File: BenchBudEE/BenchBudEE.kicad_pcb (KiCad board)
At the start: 4 copper layers, 165.1 x 63.5 mm, 57 parts, among them K1 1461069-5, P1 24 Pin MiniFit JR, P2 CONN_3X2, P3 CONN_2, P4 12 Pin Terminal Block, P5 3 Pin TB, Q1 2N3904, U1 LTV-816S, U2 MCP3901, U3 LMT84, U4 OPA4170

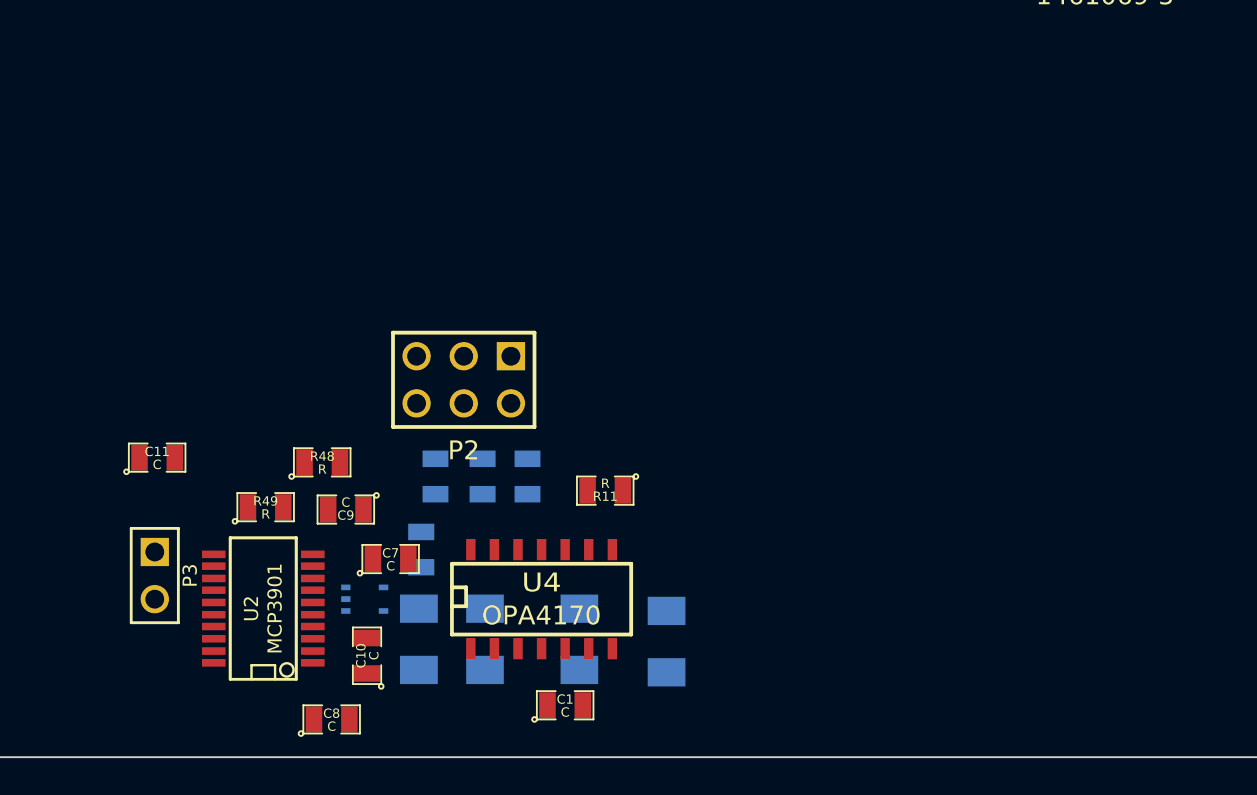
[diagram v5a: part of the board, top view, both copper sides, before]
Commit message: Roughly placed the current/fan driver module components.
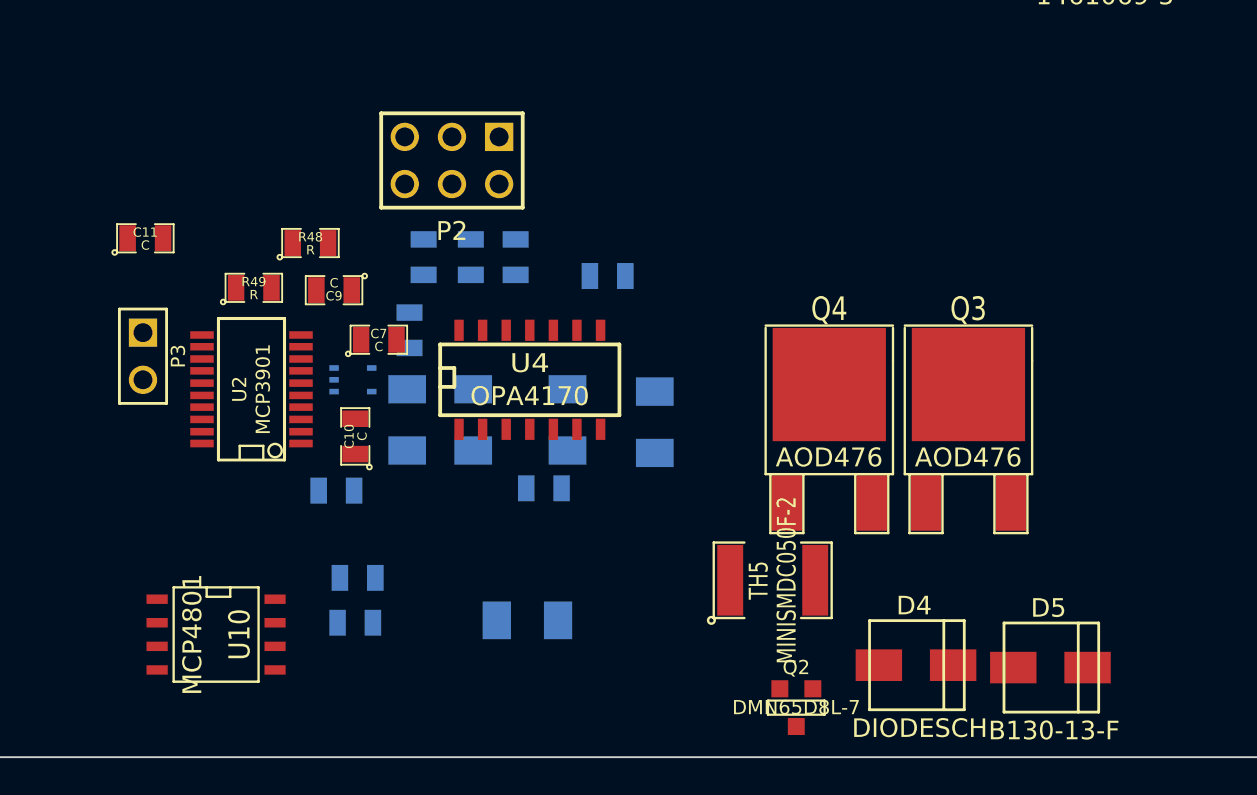
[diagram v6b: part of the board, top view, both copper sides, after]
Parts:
- added C13: C, SM0805, B.Cu at (183.0, 169.3)
- added D4: DIODESCH, SMA, F.Cu at (211.2, 171.6)
- added D5: B130-13-F, SMA, F.Cu at (218.4, 171.7)
- added Q2: DMN65D8L-7, SOT23GDS, F.Cu at (206.8, 173.9)
- added Q3: AOD476, DPAK2, F.Cu at (216.0, 162.8)
- added Q4: AOD476, DPAK2, F.Cu at (208.5, 162.8)
- added R24: R, SM0805, B.Cu at (183.1, 166.9)
- added R25: R, SM1206, B.Cu at (192.3, 169.2)
- added TH5: MINISMDC050F-2, SM1812, F.Cu at (205.5, 167.0)
- added U10: MCP4801, SO8N, F.Cu at (175.5, 169.9)
- C1, C8, R11: moved to B.Cu
- moved C8 12.3 mm to (182.0, 162.2)
- moved C11 11.8 mm to (171.7, 148.6)
- moved C7 11.8 mm to (184.3, 154.1)
- moved C9 11.8 mm to (181.9, 151.4)
- moved P2 11.8 mm to (188.2, 144.4)
- moved P3 11.8 mm to (171.6, 154.9)
- moved R10 11.8 mm to (189.4, 158.4)
- moved R12 11.8 mm to (186.7, 149.6)
- moved R13 11.8 mm to (185.9, 153.5)
- moved R44 11.8 mm to (191.6, 149.6)
- moved R45 11.8 mm to (189.2, 149.6)
- moved R48 11.8 mm to (180.6, 148.8)
- moved R49 11.8 mm to (177.5, 151.3)
- moved R7 11.8 mm to (194.4, 158.4)
- moved R8 11.8 mm to (185.8, 158.4)
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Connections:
- net /Arduino/ADC_CS_N renamed /Arduino/~ADC_CS
- ARD1 pad 13: (no net) -> N-0000059
- ARD1 pad 14: (no net) -> N-0000054

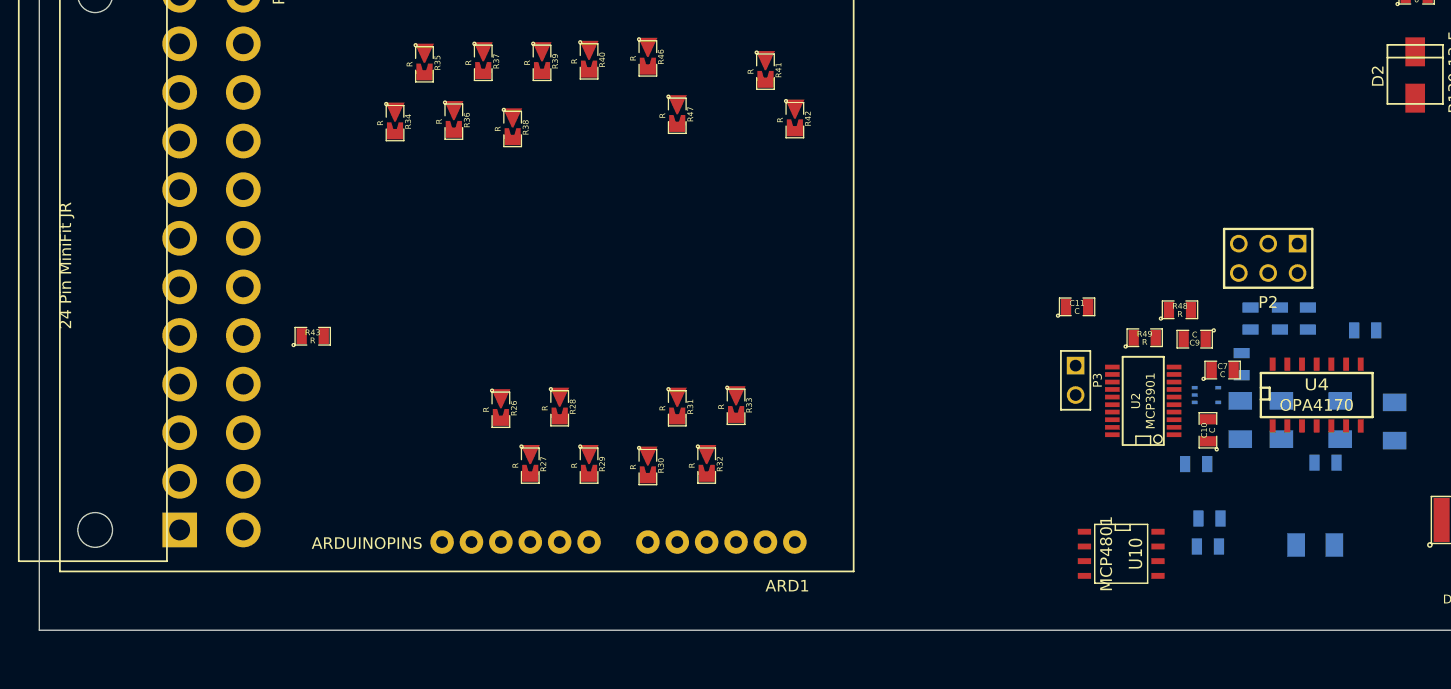
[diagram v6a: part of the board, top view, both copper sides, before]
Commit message: Roughly placed components for the Power Protection and Filtering module.
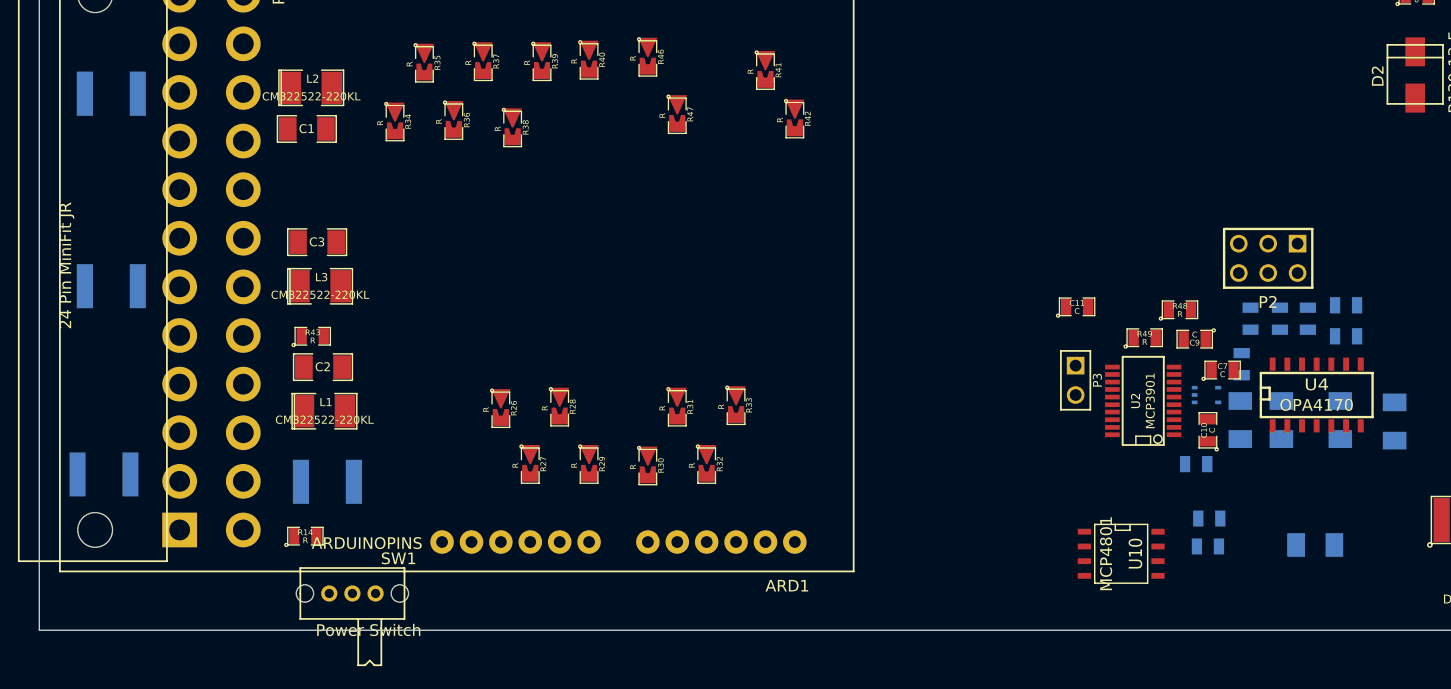
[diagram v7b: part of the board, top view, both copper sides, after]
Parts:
- added C2: C, SM1206, F.Cu at (106.6, 153.8)
- added C3: C, SM1206, F.Cu at (106.0, 143.0)
- added C6: C, SM0805, B.Cu at (194.9, 151.1)
- added L1: CM322522-220KL, SM1210L, F.Cu at (106.7, 157.6)
- added L2: CM322522-220KL, SM1210L, F.Cu at (105.5, 129.7)
- added L3: CM322522-220KL, SM1210L, F.Cu at (106.3, 146.8)
- added R14: R, SM0805, F.Cu at (105.0, 168.4)
- added SW1: Power Switch, BB_switch, F.Cu at (109.1, 173.4)
- added TH1: MINISMDC050F-2, SM1812, B.Cu at (87.6, 163.1)
- added TH2: MINISMDC050F-2, SM1812, B.Cu at (88.3, 146.8)
- added TH3: MINISMDC050F-2, SM1812, B.Cu at (88.3, 130.2)
- added TH4: MINISMDC050F-2, SM1812, B.Cu at (106.9, 163.7)
- C1: footprint SM0805 -> SM1206; moved to F.Cu
- moved C1 92.6 mm to (105.2, 133.2), turned to 180 degrees
- moved R11 2.72 mm to (194.9, 148.5)

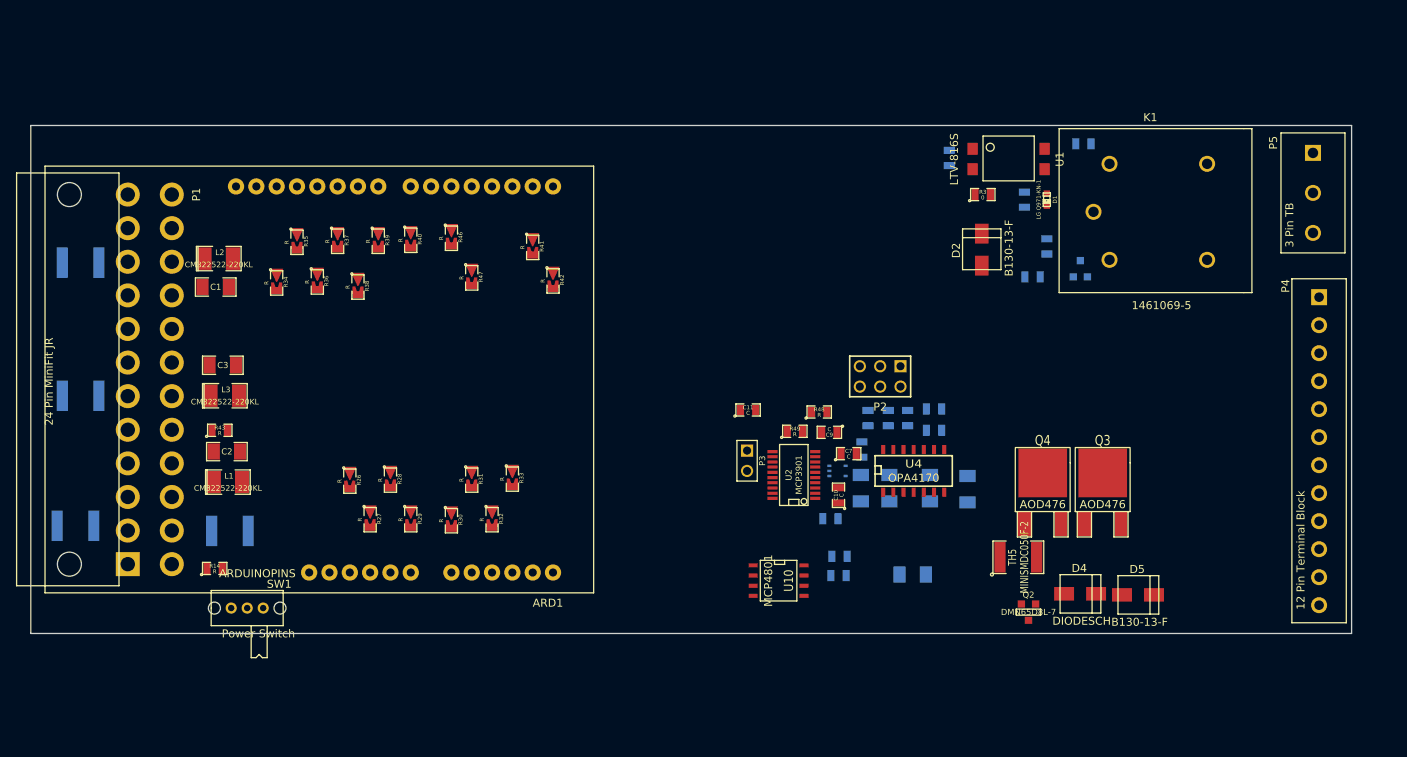
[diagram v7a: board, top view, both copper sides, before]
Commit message: Roughly placed the power modification module components.
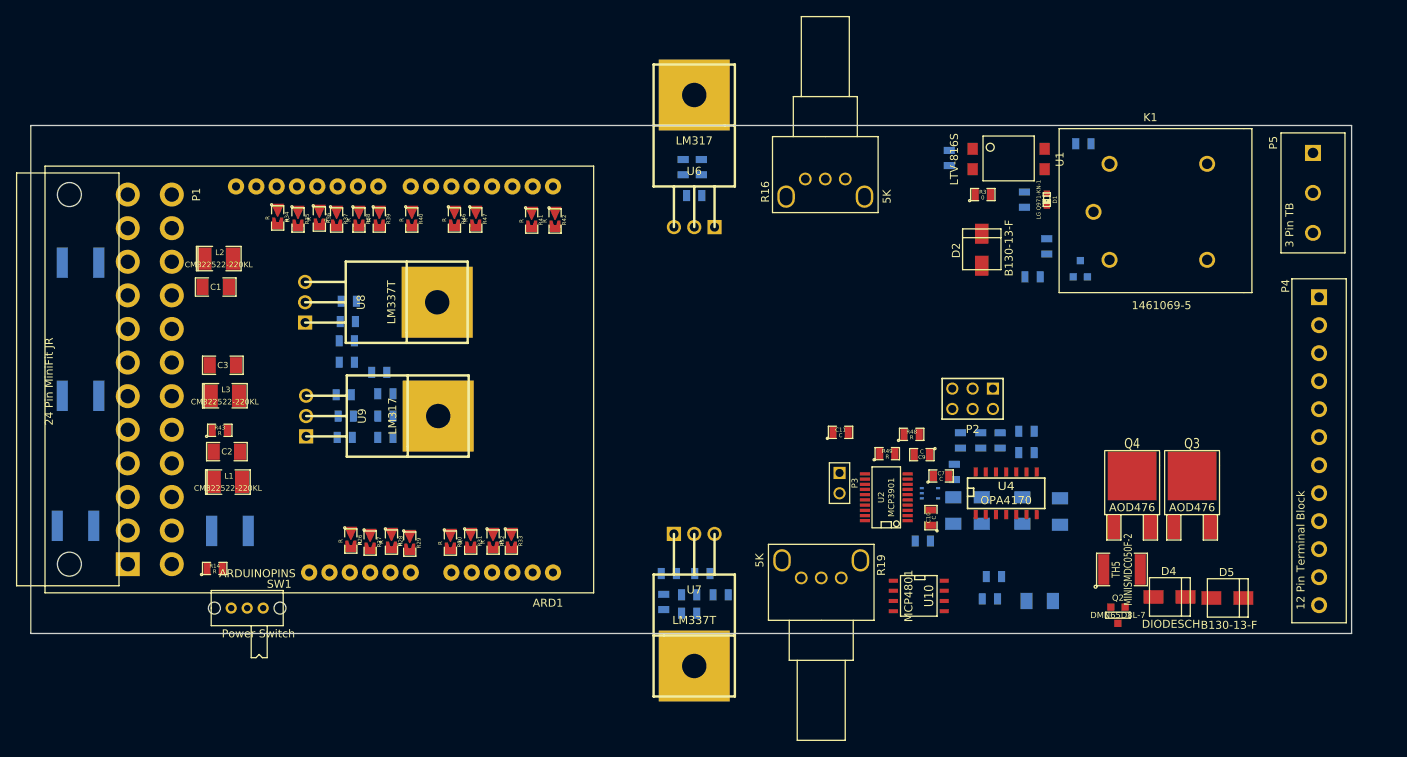
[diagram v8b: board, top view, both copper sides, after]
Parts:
- added C14: C, SM0805, B.Cu at (121.3, 152.0)
- added C15: C, SM0805, B.Cu at (126.4, 146.6)
- added C16: C, SM0805, B.Cu at (161.8, 169.0)
- added C17: C, SM0805, B.Cu at (165.0, 121.8)
- added C18: C, SM0805, B.Cu at (165.9, 118.2)
- added C19: C, SM0805, B.Cu at (121.5, 142.6)
- added C20: C, SM0805, B.Cu at (125.6, 143.9)
- added C21: C, SM0805, B.Cu at (164.3, 174.0)
- added C22: C, SM0805, B.Cu at (121.8, 135.0)
- added C23: C, SM0805, B.Cu at (121.4, 149.4)
- added C24: C, SM0805, B.Cu at (126.4, 149.4)
- added R16: 5K, EVUE3K, F.Cu at (181.4, 121.9)
- added R17: 715, SM0805, B.Cu at (163.6, 118.2)
- added R18: 715, SM0805, B.Cu at (161.2, 172.6)
- added R19: 5K, EVUE3K, F.Cu at (180.8, 167.4)
- added R20: R, SM0805, B.Cu at (129.7, 150.7)
- added R21: R, SM0805, B.Cu at (126.4, 152.0)
- added R22: R, SM0805, B.Cu at (168.3, 171.7)
- added R23: R, SM0805, B.Cu at (164.3, 171.7)
- added R52: R, SM0805, B.Cu at (121.5, 140.0)
- added R53: R, SM0805, B.Cu at (121.7, 137.5)
- added R54: R, SM0805, B.Cu at (121.2, 146.7)
- added R55: R, SM0805, B.Cu at (166.0, 169.0)
- added U6: LM317, TO220, F.Cu at (165.0, 125.7)
- added U7: LM337T, TO220, F.Cu at (165.0, 164.1)
- added U8: LM337T, TO220, F.Cu at (116.3, 135.1)
- added U9: LM317, TO220, F.Cu at (116.5, 149.4)
- moved R24 19.5 mm to (202.4, 169.4)
- moved C13 19.1 mm to (201.9, 172.2)
- moved U10 17.6 mm to (193.0, 171.8)
- moved R25 16.2 mm to (208.2, 172.5)
- moved TH5 13.0 mm to (218.4, 168.5)
- moved C6 11.9 mm to (206.5, 153.9)
- moved C7 11.9 mm to (195.8, 156.8)
- moved R11 11.9 mm to (206.5, 151.3)
- moved R12 11.9 mm to (198.2, 152.4)
- moved R45 11.9 mm to (200.8, 152.4)
- moved R48 11.9 mm to (192.2, 151.6)
- moved R8 11.9 mm to (197.4, 161.2)
- moved R13 11.9 mm to (197.5, 156.3)
- moved R49 11.9 mm to (189.1, 154.1)
- moved R9 11.9 mm to (210.7, 161.3)
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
